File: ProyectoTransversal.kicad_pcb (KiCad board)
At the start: 2 copper layers, 25 parts, among them J1 Conn_01x19, J2 Conn_01x19, J3 Screw_Terminal_01x02, J4 Screw_Terminal_01x02, J5 Conn_01x04, K1 Relay_SPDT, Q1 IRLZ44N, Q2 BC547, U1 DS18B20, U2 LM2596S-5

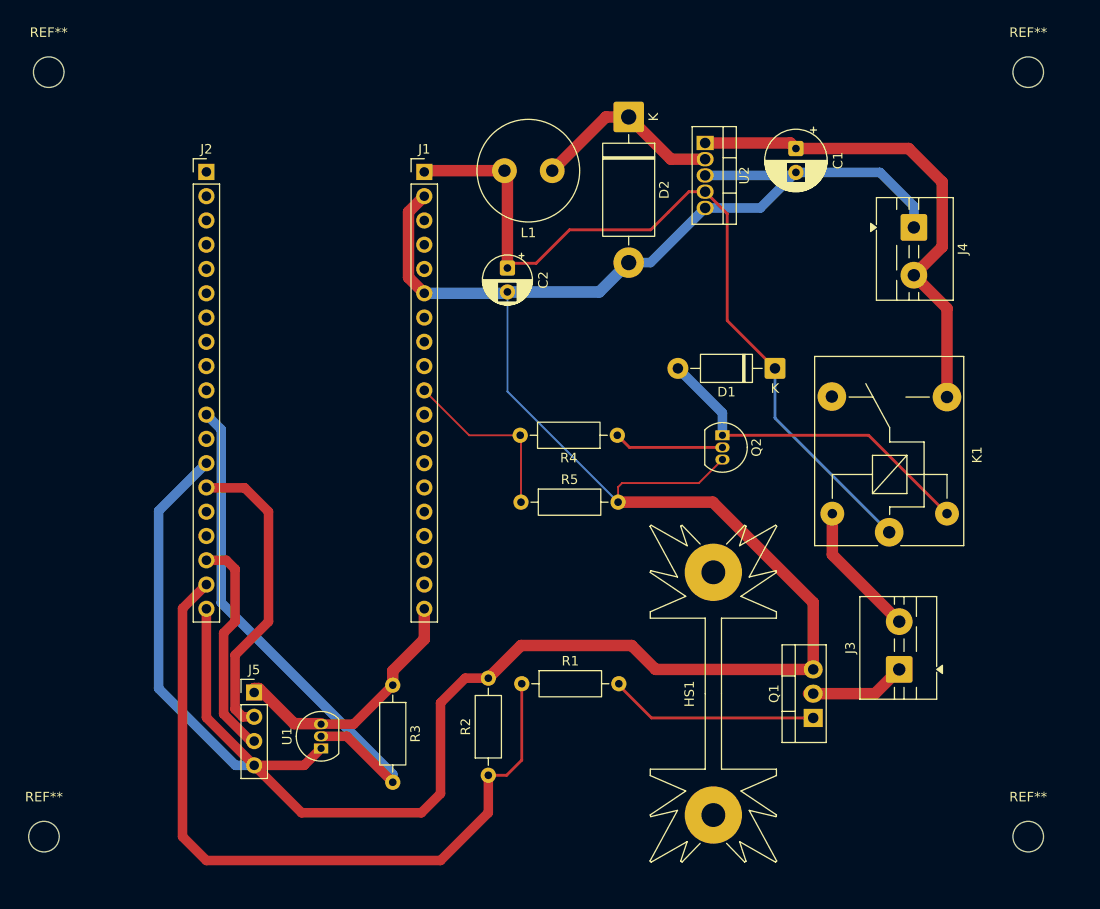
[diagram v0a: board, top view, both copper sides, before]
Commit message: Rework vias to transform PCB into one-sided
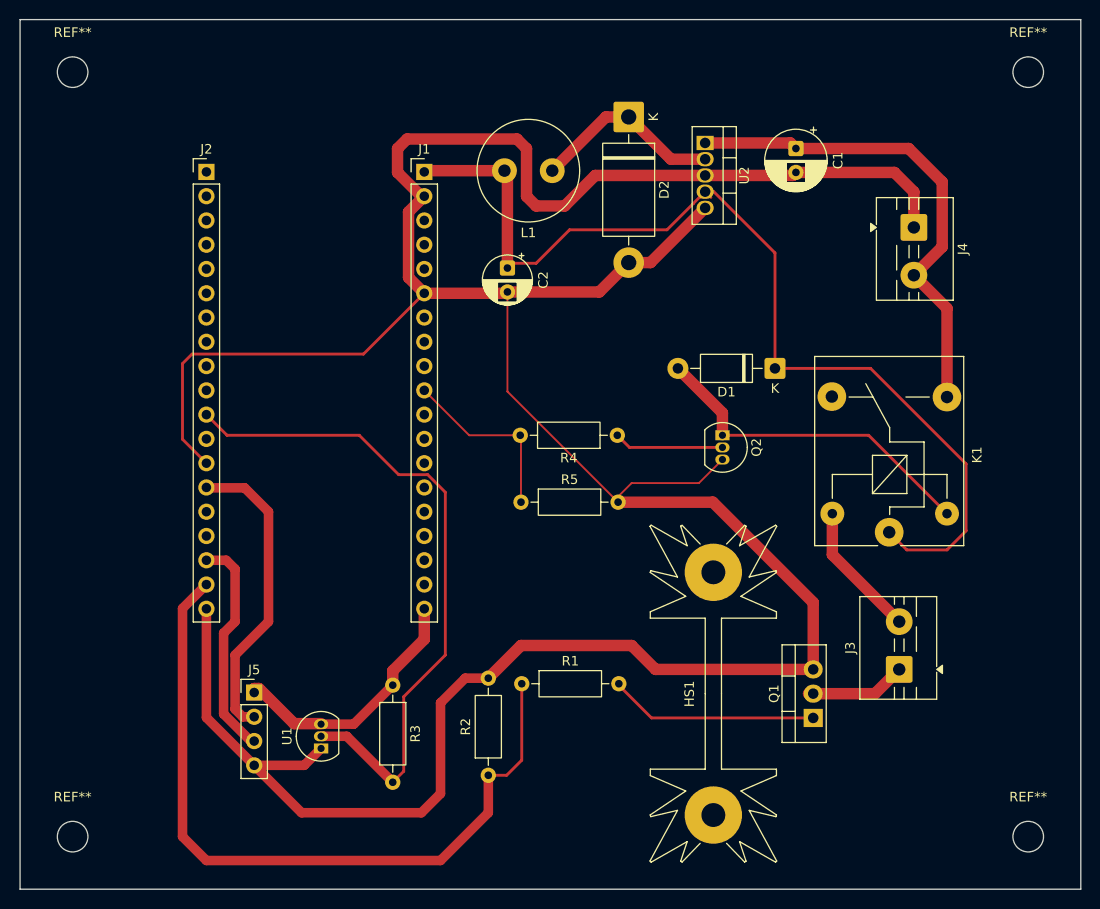
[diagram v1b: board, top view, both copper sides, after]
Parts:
- moved REF** 3.00 mm to (130.0, 143.5)
- moved REF** 2.50 mm to (130.0, 63.5)
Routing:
- net GND: track 292.9 -> 329.7 mm
- net /V_reg: track 86.4 -> 105.6 mm
- net /sensor_temp: track 56.0 -> 70.5 mm
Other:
- board outline added: 111 x 91 mm

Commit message: Change C1 C2 and R footprints
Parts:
- C1: footprint Capacitor_THT:CP_Radial_D6.3mm_P2.50mm -> Capacitor_SMD:CP_Elec_6.3x7.7
- C2: footprint Capacitor_THT:CP_Radial_D5.0mm_P2.50mm -> Capacitor_SMD:CP_Elec_8x10.5
- R1, R2, R3, R4, R5: footprint Resistor_THT:R_Axial_DIN0207_L6.3mm_D2.5mm_P10.16mm_Horizontal -> Resistor_SMD:R_1206_3216Metric
- moved R3 4.38 mm to (163.0, 132.0)
- moved R1 4.00 mm to (181.0, 127.5)
- moved C2 3.30 mm to (175.5, 87.3)
- moved C1 1.81 mm to (207.5, 71.5)
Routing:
- net /GATE: track 21.4 -> 26.0 mm
- net /12V: track 51.7 -> 53.4 mm
- net /PWM_OUT: track 78.6 -> 79.6 mm
- net GND: track 329.7 -> 328.7 mm

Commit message: Modify vias
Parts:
- moved R5 7.02 mm to (177.5, 101.5)
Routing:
- net GND: track 328.7 -> 314.3 mm
- net /CMD_Relay: track 19.2 -> 11.1 mm
- net /sensor_temp: track 70.5 -> 64.9 mm
- net /3V3: track 27.5 -> 28.9 mm
- net /PWM_OUT: track 79.6 -> 78.5 mm

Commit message: Finish wiring SMD resistors
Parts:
- moved R4 7.24 mm to (180.0, 99.5)
- moved R5 3.59 mm to (180.0, 104.0)
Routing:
- net Net-(Q2-B): track 11.5 -> 17.9 mm
- net /CMD_Relay: track 11.1 -> 17.4 mm
- net GND: track 314.3 -> 319.8 mm
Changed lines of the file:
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@@
 	(footprint "Resistor_SMD:R_1206_3216Metric"
 		(layer "F.Cu")
-		(at 187 101.5 180)
+		(at 180.0375 99.5 180)
 		(descr "Resistor SMD 1206 (3216 Metric), square (rectangular) end terminal, IPC-7351 nominal, (Body size source: IPC-SM-782 page 72, https://www.pcb-3d.com/wordpress/wp-content/uploads/ipc-sm-782a_amendment_1_and_2.pdf)")
 		(tags "resistor")
@@
 	(footprint "Resistor_SMD:R_1206_3216Metric"
 		(layer "F.Cu")
-		(at 177.4625 101.5)
+		(at 180.0375 104)
 		(descr "Resistor SMD 1206 (3216 Metric), square (rectangular) end terminal, IPC-7351 nominal, (Body size source: IPC-SM-782 page 72, https://www.pcb-3d.com/wordpress/wp-content/uploads/ipc-sm-782a_amendment_1_and_2.pdf)")
 		(tags "resistor")
@@
 			(at 0 -1.83 0)
 			(layer "F.SilkS")
+			(hide yes)
 			(effects
 				(font
@@
 	)
 	(segment
-		(start 188.5 106.5)
-		(end 195.54 106.5)
+		(start 176 97.5)
+		(end 179.5 97.5)
 		(width 0.2)
 		(layer "F.Cu")
@@
 	)
 	(segment
+		(start 180 102.5)
+		(end 181.5 104)
+		(width 0.2)
+		(layer "F.Cu")
+		(net "GND")
+	)
+	(segment
 		(start 166.8 86.64)
 		(end 165.15 84.99)
@@
 	)
 	(segment
-		(start 180.62 91)
-		(end 188.19 83.43)
-		(width 1.2)
+		(start 182.69125 106.5)
+		(end 195.54 106.5)
+		(width 0.2)
 		(layer "F.Cu")
 		(net "GND")
 	)
 	(segment
-		(start 178.5 98)
-		(end 176.58 98)
-		(width 0.2)
+		(start 180.62 91)
+		(end 188.19 83.43)
+		(width 1.2)
 		(layer "F.Cu")
 		(net "GND")
@@
 	)
 	(segment
-		(start 178.925 98.425)
-		(end 178.5 98)
-		(width 0.2)
-		(layer "F.Cu")
-		(net "GND")
-	)
-	(segment
 		(start 165 70.5)
 		(end 164 71.5)
@@
 	)
 	(segment
-		(start 178.925 101.5)
-		(end 178.925 98.425)
-		(width 0.2)
-		(layer "F.Cu")
-		(net "GND")
-	)
-	(segment
 		(start 166.8 87.2)
 		(end 166.8 86.64)
@@
 	)
 	(segment
+		(start 195.54 106.5)
+		(end 198 104.04)
+		(width 0.2)
+		(layer "F.Cu")
+		(net "GND")
+	)
+	(segment
 		(start 177.5 71.5)
 		(end 176.5 70.5)
@@
 	)
 	(segment
+		(start 179.5 97.5)
+		(end 180 98)
+		(width 0.2)
+		(layer "F.Cu")
+		(net "GND")
+	)
+	(segment
 		(start 190.47 83.43)
 		(end 188.19 83.43)
@@
 	)
 	(segment
+		(start 181.5 104)
+		(end 181.5 105.30875)
+		(width 0.2)
+		(layer "F.Cu")
+		(net "GND")
+	)
+	(segment
 		(start 218.0325 79.75)
 		(end 218.0325 76.0325)
@@
 	)
 	(segment
-		(start 175.5 96.92)
-		(end 175.5 91)
+		(start 180 98)
+		(end 180 102.5)
 		(width 0.2)
 		(layer "F.Cu")
@@
 	)
 	(segment
-		(start 176.58 98)
-		(end 175.5 96.92)
+		(start 175.5 97)
+		(end 176 97.5)
 		(width 0.2)
 		(layer "F.Cu")
@@
 	)
 	(segment
+		(start 175.5 91)
+		(end 175.5 97)
+		(width 0.2)
+		(layer "F.Cu")
+		(net "GND")
+	)
+	(segment
 		(start 149 136.04)
 		(end 154.23 136.04)
@@
 	)
 	(segment
-		(start 181.27125 107.92)
-		(end 187.08 107.92)
-		(width 0.2)
-		(layer "F.Cu")
-		(net "GND")
-	)
-	(segment
-		(start 195.54 106.5)
-		(end 198 104.04)
-		(width 0.2)
-		(layer "F.Cu")
-		(net "GND")
-	)
-	(segment
 		(start 218.0325 76.0325)
 		(end 215.99238 73.99238)
@@
 	)
 	(segment
-		(start 187.08 107.92)
-		(end 188.5 106.5)
-		(width 0.2)
+		(start 176.92 123.5)
+		(end 188.5 123.5)
+		(width 1.2)
 		(layer "F.Cu")
 		(net "GND")
 	)
 	(segment
-		(start 176.92 123.5)
-		(end 188.5 123.5)
-		(width 1.2)
+		(start 181.5 105.30875)
+		(end 182.69125 106.5)
+		(width 0.2)
 		(layer "F.Cu")
 		(net "GND")
@@
 	)
 	(segment
-		(start 171.5 101.5)
+		(start 169.5 99.5)
 		(end 166.8 96.8)
 		(width 0.2)
@@
 	)
 	(segment
-		(start 176 101.5)
-		(end 171.5 101.5)
+		(start 178.575 99.5)
+		(end 169.5 99.5)
+		(width 0.2)
+		(layer "F.Cu")
+		(net "/CMD_Relay")
+	)
+	(segment
+		(start 178.575 104)
+		(end 178.575 99.5)
 		(width 0.2)
 		(layer "F.Cu")
@@
 	)
 	(segment
-		(start 187 101.5)
-		(end 188.27 102.77)
+		(start 181.5 99.5)
+		(end 185 99.5)
 		(width 0.3)
 		(layer "F.Cu")
@@
 		(width 0.3)
 		(layer "F.Cu")
+		(net "Net-(Q2-B)")
+	)
+	(segment
+		(start 185 99.5)
+		(end 188.27 102.77)
+		(width 0.3)
+		(layer "F.Cu")

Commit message: Actualizacion footprints de esquematico
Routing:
- net GND: track 319.8 -> 326.3 mm
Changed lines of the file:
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@@
+	)
+	(segment
+		(start 202 106.5)
+		(end 206 110.5)
+		(width 0.2)
+		(layer "F.Cu")
+		(net "GND")
 	)
 	(segment
@@
 	)
 	(segment
+		(start 206 117.5)
+		(end 207.5 119)
+		(width 0.2)
+		(layer "F.Cu")
+		(net "GND")
+	)
+	(segment
 		(start 180 102.5)
 		(end 181.5 104)
@@
 	)
 	(segment
-		(start 182.69125 106.5)
-		(end 195.54 106.5)
+		(start 207.5 119)
+		(end 207.5 126)
 		(width 0.2)
 		(layer "F.Cu")
@@
 	)
 	(segment
+		(start 181.5 104)
+		(end 181.5 105.5)
+		(width 0.2)
+		(layer "F.Cu")
+		(net "GND")
+	)
+	(segment
 		(start 165.15 84.99)
 		(end 165.15 78.13)
@@
 	)
 	(segment
-		(start 197 108.5)
-		(end 207.5 119)
-		(width 1.2)
+		(start 181.5 105.5)
+		(end 182.5 106.5)
+		(width 0.2)
 		(layer "F.Cu")
 		(net "GND")
@@
 	)
 	(segment
+		(start 177.5 71.5)
+		(end 176.5 70.5)
+		(width 1.2)
+		(layer "F.Cu")
+		(net "GND")
+	)
+	(segment
+		(start 175 91)
+		(end 170.64 86.64)
+		(width 1.2)
+		(layer "F.Cu")
+		(net "GND")
+	)
+	(segment
+		(start 175.5 91)
+		(end 180.62 91)
+		(width 1.2)
+		(layer "F.Cu")
+		(net "GND")
+	)
+	(segment
+		(start 191 126)
+		(end 207.5 126)
+		(width 1.2)
+		(layer "F.Cu")
+		(net "GND")
+	)
+	(segment
+		(start 179.5 97.5)
+		(end 180 98)
+		(width 0.2)
+		(layer "F.Cu")
+		(net "GND")
+	)
+	(segment
+		(start 195.54 106.5)
+		(end 202 106.5)
+		(width 0.2)
+		(layer "F.Cu")
+		(net "GND")
+	)
+	(segment
+		(start 190.47 83.43)
+		(end 188.19 83.43)
+		(width 1.2)
+		(layer "F.Cu")
+		(net "GND")
+	)
+	(segment
+		(start 218.0325 79.75)
+		(end 218.0325 76.0325)
+		(width 1.2)
+		(layer "F.Cu")
+		(net "GND")
+	)
+	(segment
+		(start 153.96 141)
+		(end 149 136.04)
+		(width 1)
+		(layer "F.Cu")
+		(net "GND")
+	)
+	(segment
+		(start 176.5 70.5)
+		(end 165 70.5)
+		(width 1.2)
+		(layer "F.Cu")
+		(net "GND")
+	)
+	(segment
+		(start 165.15 78.13)
+		(end 166.8 76.48)
+		(width 1.2)
+		(layer "F.Cu")
+		(net "GND")
+	)
+	(segment
+		(start 180 98)
+		(end 180 102.5)
+		(width 0.2)
+		(layer "F.Cu")
+		(net "GND")
+	)
+	(segment
+		(start 175.5 97)
+		(end 176 97.5)
+		(width 0.2)
+		(layer "F.Cu")
+		(net "GND")
+	)
+	(segment
+		(start 141.5 101.92)
+		(end 141.5 94)
+		(width 0.3)
+		(layer "F.Cu")
+		(net "GND")
+	)
+	(segment
+		(start 178.5 77.5)
+		(end 177.5 76.5)
+		(width 1.2)
+		(layer "F.Cu")
+		(net "GND")
+	)
+	(segment
+		(start 141.5 94)
+		(end 142.5 93)
+		(width 0.3)
+		(layer "F.Cu")
+		(net "GND")
+	)
+	(segment
+		(start 188.5 123.5)
+		(end 191 126)
+		(width 1.2)
+		(layer "F.Cu")
+		(net "GND")
+	)
+	(segment
+		(start 164 71.5)
+		(end 164 74)
+		(width 1.2)
+		(layer "F.Cu")
+		(net "GND")
+	)
+	(segment
+		(start 175.5 91)
+		(end 175.5 97)
+		(width 0.2)
+		(layer "F.Cu")
+		(net "GND")
+	)
+	(segment
+		(start 149 136.04)
+		(end 154.23 136.04)
+		(width 1)
+		(layer "F.Cu")
+		(net "GND")
+	)
+	(segment
+		(start 166.48 76.48)
+		(end 166.8 76.48)
+		(width 1.2)
+		(layer "F.Cu")
+		(net "GND")
+	)
+	(segment
 		(start 195.54 106.5)
 		(end 198 104.04)
@@
 	)
 	(segment
-		(start 177.5 71.5)
-		(end 176.5 70.5)
-		(width 1.2)
-		(layer "F.Cu")
-		(net "GND")
-	)
-	(segment
-		(start 175 91)
-		(end 170.64 86.64)
-		(width 1.2)
-		(layer "F.Cu")
-		(net "GND")
-	)
-	(segment
-		(start 175.5 91)
-		(end 180.62 91)
-		(width 1.2)
-		(layer "F.Cu")
-		(net "GND")
-	)
-	(segment
-		(start 191 126)
-		(end 207.5 126)
-		(width 1.2)
-		(layer "F.Cu")
-		(net "GND")
-	)
-	(segment
-		(start 179.5 97.5)
-		(end 180 98)
-		(width 0.2)
-		(layer "F.Cu")
-		(net "GND")
-	)
-	(segment
-		(start 190.47 83.43)
-		(end 188.19 83.43)
-		(width 1.2)
-		(layer "F.Cu")
-		(net "GND")
-	)
-	(segment
-		(start 181.5 104)
-		(end 181.5 105.30875)
-		(width 0.2)
-		(layer "F.Cu")
-		(net "GND")
-	)
-	(segment
-		(start 218.0325 79.75)
-		(end 218.0325 76.0325)
-		(width 1.2)
-		(layer "F.Cu")
-		(net "GND")
-	)
-	(segment
-		(start 153.96 141)
-		(end 149 136.04)
-		(width 1)
-		(layer "F.Cu")
-		(net "GND")
-	)
-	(segment
-		(start 176.5 70.5)
-		(end 165 70.5)
-		(width 1.2)
-		(layer "F.Cu")
-		(net "GND")
-	)
-	(segment
-		(start 165.15 78.13)
-		(end 166.8 76.48)
-		(width 1.2)
-		(layer "F.Cu")
-		(net "GND")
-	)
-	(segment
-		(start 180 98)
-		(end 180 102.5)
-		(width 0.2)
-		(layer "F.Cu")
-		(net "GND")
-	)
-	(segment
-		(start 175.5 97)
-		(end 176 97.5)
-		(width 0.2)
-		(layer "F.Cu")
-		(net "GND")
-	)
-	(segment
-		(start 141.5 101.92)
-		(end 141.5 94)
-		(width 0.3)
-		(layer "F.Cu")
-		(net "GND")
-	)
-	(segment
-		(start 178.5 77.5)
-		(end 177.5 76.5)
-		(width 1.2)
-		(layer "F.Cu")
-		(net "GND")
-	)
-	(segment
-		(start 141.5 94)
-		(end 142.5 93)
-		(width 0.3)
-		(layer "F.Cu")
-		(net "GND")
-	)
-	(segment
-		(start 188.5 123.5)
-		(end 191 126)
-		(width 1.2)
-		(layer "F.Cu")
-		(net "GND")
-	)
-	(segment
-		(start 164 71.5)
-		(end 164 74)
-		(width 1.2)
-		(layer "F.Cu")
-		(net "GND")
-	)
-	(segment
-		(start 175.5 91)
-		(end 175.5 97)
-		(width 0.2)
-		(layer "F.Cu")
-		(net "GND")
-	)
-	(segment
-		(start 149 136.04)
-		(end 154.23 136.04)
-		(width 1)
-		(layer "F.Cu")
-		(net "GND")
-	)
-	(segment
-		(start 166.48 76.48)
-		(end 166.8 76.48)
-		(width 1.2)
-		(layer "F.Cu")
-		(net "GND")
-	)
-	(segment
 		(start 218.0325 76.0325)
 		(end 215.99238 73.99238)
@@
 	)
 	(segment
+		(start 182.5 106.5)
+		(end 195.54 106.5)
+		(width 0.2)
+		(layer "F.Cu")
+		(net "GND")
+	)
+	(segment
 		(start 176.92 123.5)
 		(end 188.5 123.5)
@@
 	)
 	(segment
-		(start 181.5 105.30875)
-		(end 182.69125 106.5)
-		(width 0.2)
-		(layer "F.Cu")
-		(net "GND")
-	)
-	(segment
-		(start 207.5 119)
-		(end 207.5 126)
-		(width 1.2)
-		(layer "F.Cu")
-		(net "GND")
+		(start 206 110.5)
+		(end 206 117.5)
+		(width 0.2)
+		(layer "F.Cu")
+		(net "GND")

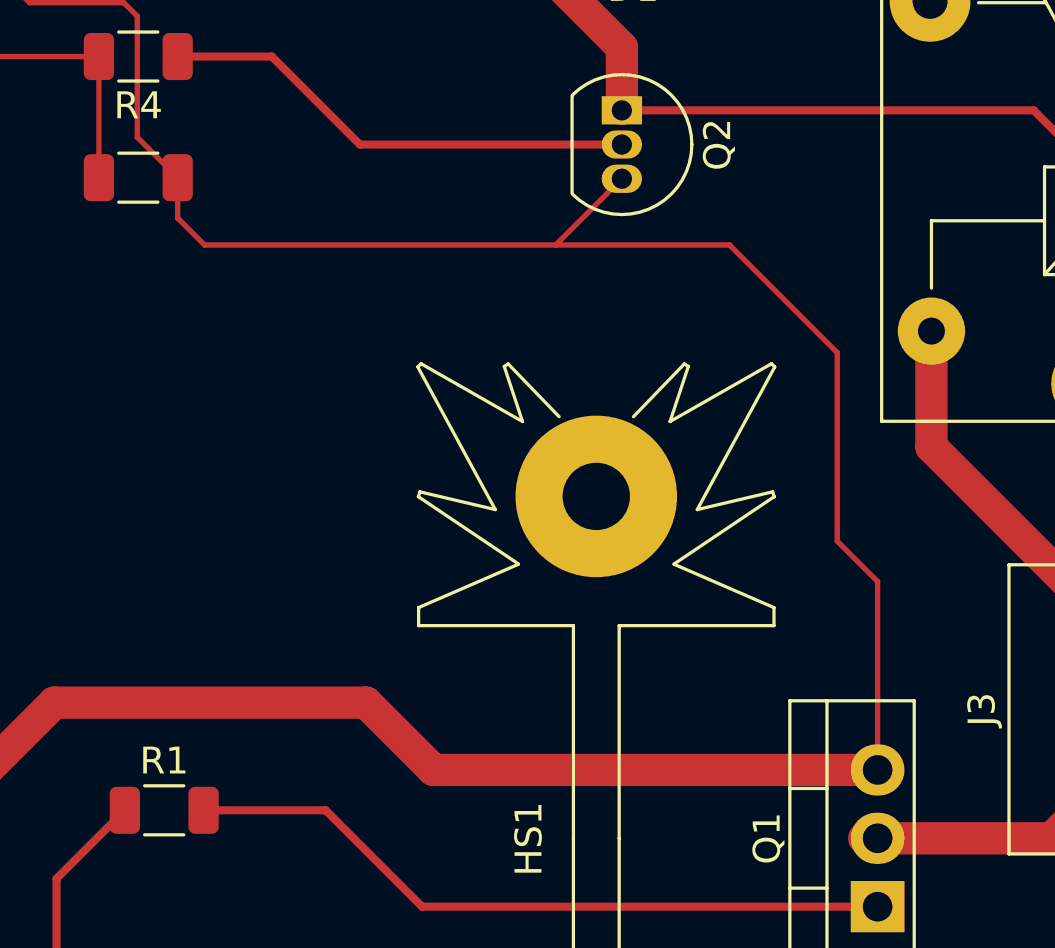
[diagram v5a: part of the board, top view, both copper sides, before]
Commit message: Fix GND width
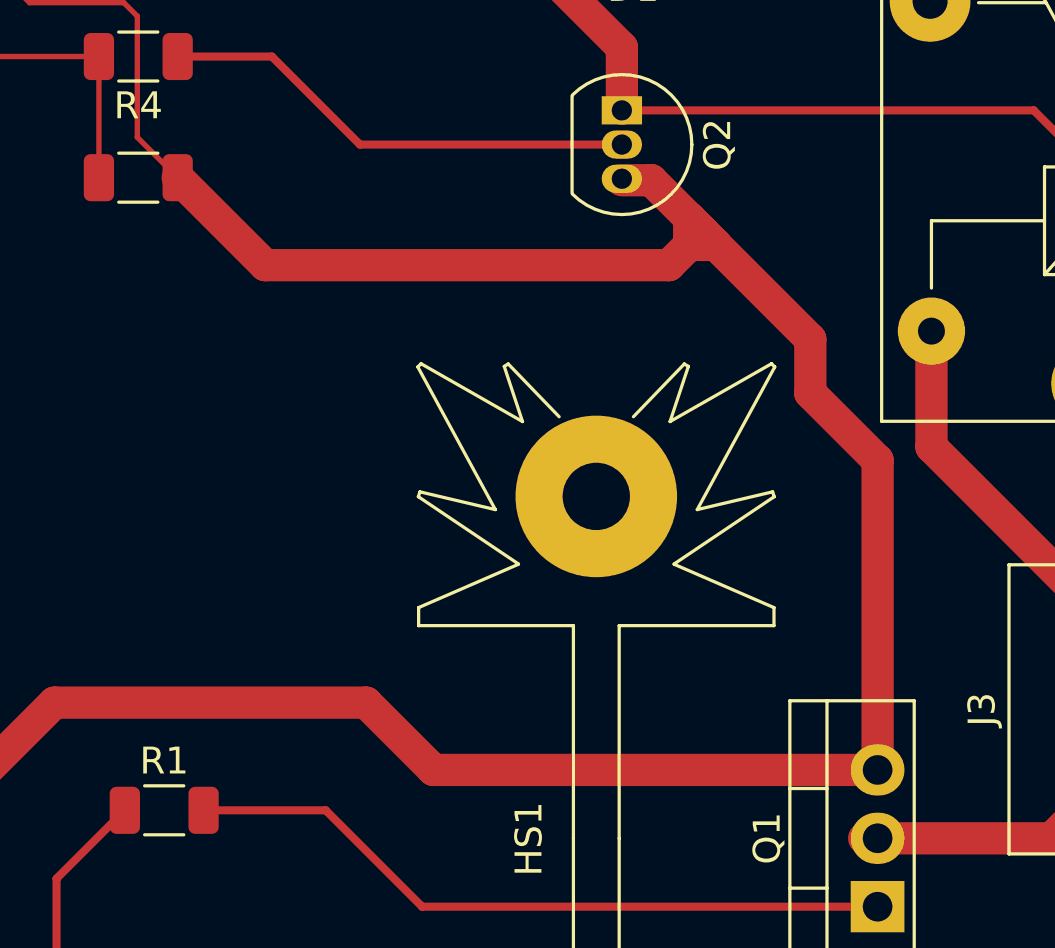
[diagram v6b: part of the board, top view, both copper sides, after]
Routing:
- net GND: track 326.3 -> 329.2 mm
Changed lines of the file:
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@@
-	)
-	(segment
-		(start 202 106.5)
-		(end 206 110.5)
-		(width 0.2)
-		(layer "F.Cu")
-		(net "GND")
 	)
 	(segment
@@
 	)
 	(segment
+		(start 207.5 114.5)
+		(end 205 112)
+		(width 1.2)
+		(layer "F.Cu")
+		(net "GND")
+	)
+	(segment
+		(start 201.5 106.5)
+		(end 200.5 105.5)
+		(width 1.2)
+		(layer "F.Cu")
+		(net "GND")
+	)
+	(segment
 		(start 176 97.5)
 		(end 179.5 97.5)
@@
 	)
 	(segment
+		(start 200.5 106.5)
+		(end 199.75 107.25)
+		(width 1.2)
+		(layer "F.Cu")
+		(net "GND")
+	)
+	(segment
 		(start 161 93)
 		(end 166.8 87.2)
@@
 	)
 	(segment
-		(start 206 117.5)
-		(end 207.5 119)
-		(width 0.2)
-		(layer "F.Cu")
-		(net "GND")
-	)
-	(segment
 		(start 180 102.5)
 		(end 181.5 104)
@@
 	)
 	(segment
-		(start 207.5 119)
-		(end 207.5 126)
-		(width 0.2)
-		(layer "F.Cu")
-		(net "GND")
-	)
-	(segment
 		(start 180.62 91)
 		(end 188.19 83.43)
@@
 	)
 	(segment
-		(start 181.5 104)
-		(end 181.5 105.5)
-		(width 0.2)
-		(layer "F.Cu")
-		(net "GND")
-	)
-	(segment
 		(start 165.15 84.99)
 		(end 165.15 78.13)
@@
 	)
 	(segment
-		(start 181.5 105.5)
-		(end 182.5 106.5)
-		(width 0.2)
-		(layer "F.Cu")
-		(net "GND")
-	)
-	(segment
 		(start 166.8 87.2)
 		(end 166.8 86.64)
@@
 	)
 	(segment
+		(start 200.5 106.5)
+		(end 201.5 106.5)
+		(width 1.2)
+		(layer "F.Cu")
+		(net "GND")
+	)
+	(segment
 		(start 179.5 97.5)
 		(end 180 98)
@@
 	)
 	(segment
-		(start 195.54 106.5)
-		(end 202 106.5)
-		(width 0.2)
+		(start 205 112)
+		(end 205 110)
+		(width 1.2)
+		(layer "F.Cu")
+		(net "GND")
+	)
+	(segment
+		(start 207.5 126)
+		(end 207.5 114.5)
+		(width 1.2)
 		(layer "F.Cu")
 		(net "GND")
@@
 	)
 	(segment
+		(start 201 106)
+		(end 199.095 104.095)
+		(width 1.2)
+		(layer "F.Cu")
+		(net "GND")
+	)
+	(segment
 		(start 176.5 70.5)
 		(end 165 70.5)
@@
 	)
 	(segment
+		(start 199.75 107.25)
+		(end 184.75 107.25)
+		(width 1.2)
+		(layer "F.Cu")
+		(net "GND")
+	)
+	(segment
 		(start 141.5 101.92)
 		(end 141.5 94)
@@
 	)
 	(segment
+		(start 199.095 104.095)
+		(end 198 104.095)
+		(width 1.2)
+		(layer "F.Cu")
+		(net "GND")
+	)
+	(segment
 		(start 149 136.04)
 		(end 154.23 136.04)
@@
 	)
 	(segment
-		(start 195.54 106.5)
-		(end 198 104.04)
-		(width 0.2)
+		(start 200.5 105.5)
+		(end 200.5 106.5)
+		(width 1.2)
+		(layer "F.Cu")
+		(net "GND")
+	)
+	(segment
+		(start 205 110)
+		(end 201 106)
+		(width 1.2)
 		(layer "F.Cu")
 		(net "GND")
@@
 	)
 	(segment
+		(start 184.75 107.25)
+		(end 181.5 104)
+		(width 1.2)
+		(layer "F.Cu")
+		(net "GND")
+	)
+	(segment
 		(start 196.19 77.71)
 		(end 190.47 83.43)
@@
 	)
 	(segment
-		(start 182.5 106.5)
-		(end 195.54 106.5)
-		(width 0.2)
-		(layer "F.Cu")
-		(net "GND")
-	)
-	(segment
 		(start 176.92 123.5)
 		(end 188.5 123.5)
@@
 		(layer "F.Cu")
 		(net "GND")
-	)
-	(segment
-		(start 206 110.5)
-		(end 206 117.5)
-		(width 0.2)
-		(layer "F.Cu")
-		(net "GND")
